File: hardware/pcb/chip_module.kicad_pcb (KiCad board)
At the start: 6 copper layers, 150 x 140 mm, 201 parts, among them J12 BTB_DAUGHTER

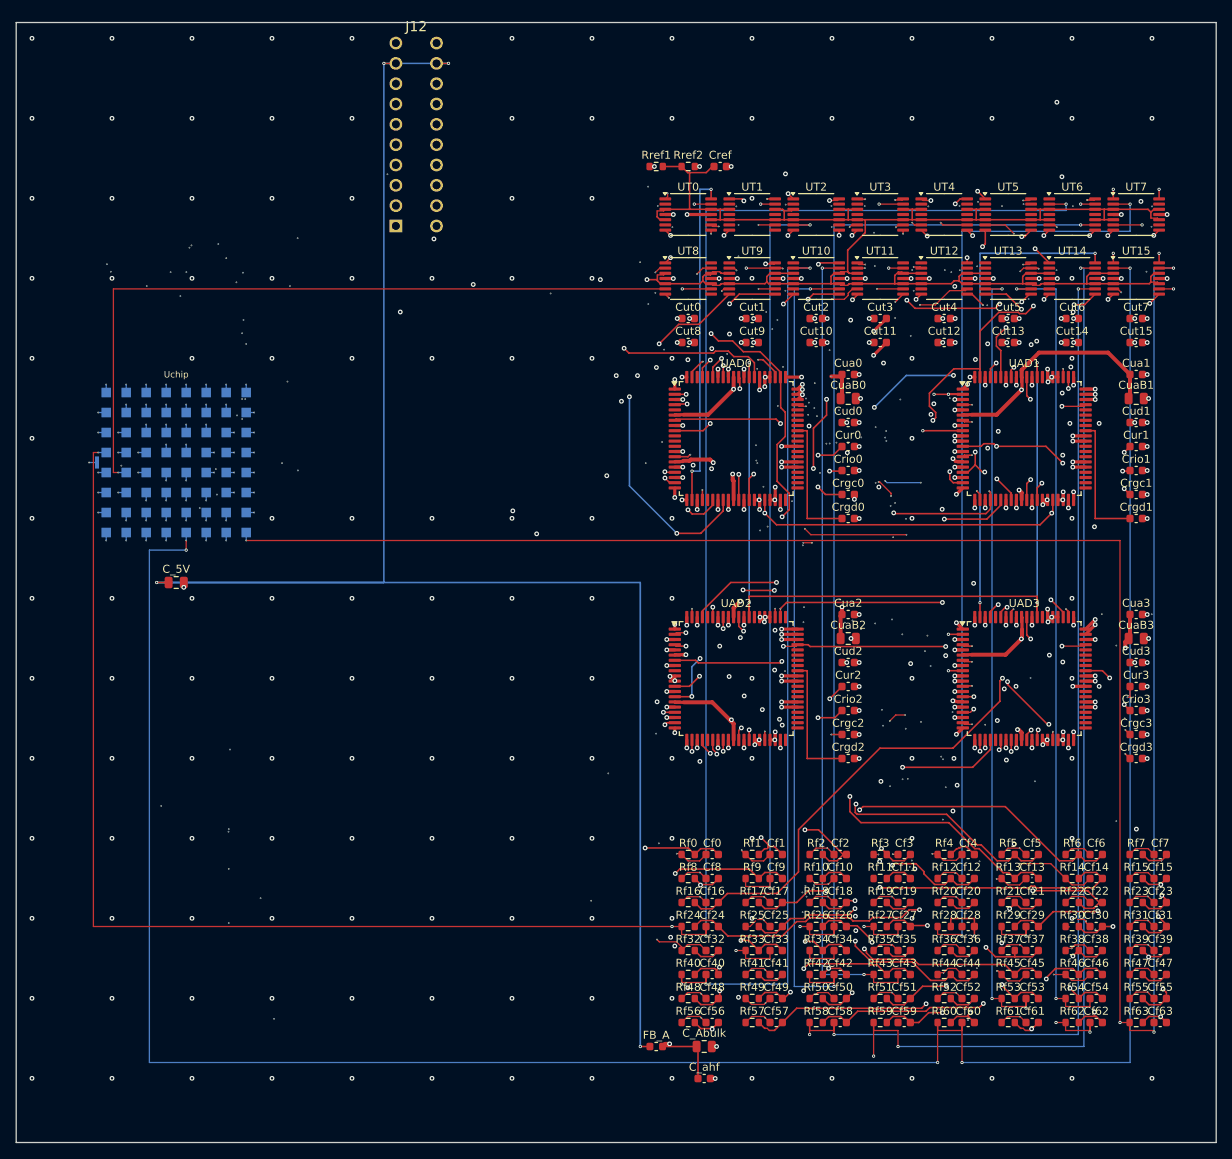
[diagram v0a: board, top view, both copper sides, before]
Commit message: pcb(head): FreeRouting cycle 1 -> 139->79 split nets, DRC 0/0/0
FreeRouting 2.4.1 -mt 0 -mp 6 on the head board (worktree off pcb/head-drc-clean).
Auto-routed the 301 unrouted items -> 92 internal; after SES import + fresh
zone re-fill the real gate (_split_nets) drops 139 -> 79 split nets (all 17
adc_* closed + 43 DET_* closed; 79 DET_* remain for cycle 2).

Post-cycle cleanup (freeroute.py imports the SES; this is the fresh-process
pass after):
  - widen 32 FreeRouting sub-min tracks (0.1124 mm -> 0.15 mm Chip netclass min)
  - relax min_hole_to_hole 0.22 -> 0.20 mm (HDI-safe; 2 adjacent FreeRouting
    fanout vias DET_IN11/DET_IN18 sit 0.2034 mm apart, 0.20 clears it)

DRC: 0 violations / 0 unconnected. Ruff clean.

Co-Authored-By: Claude Code <noreply@anthropic.com>
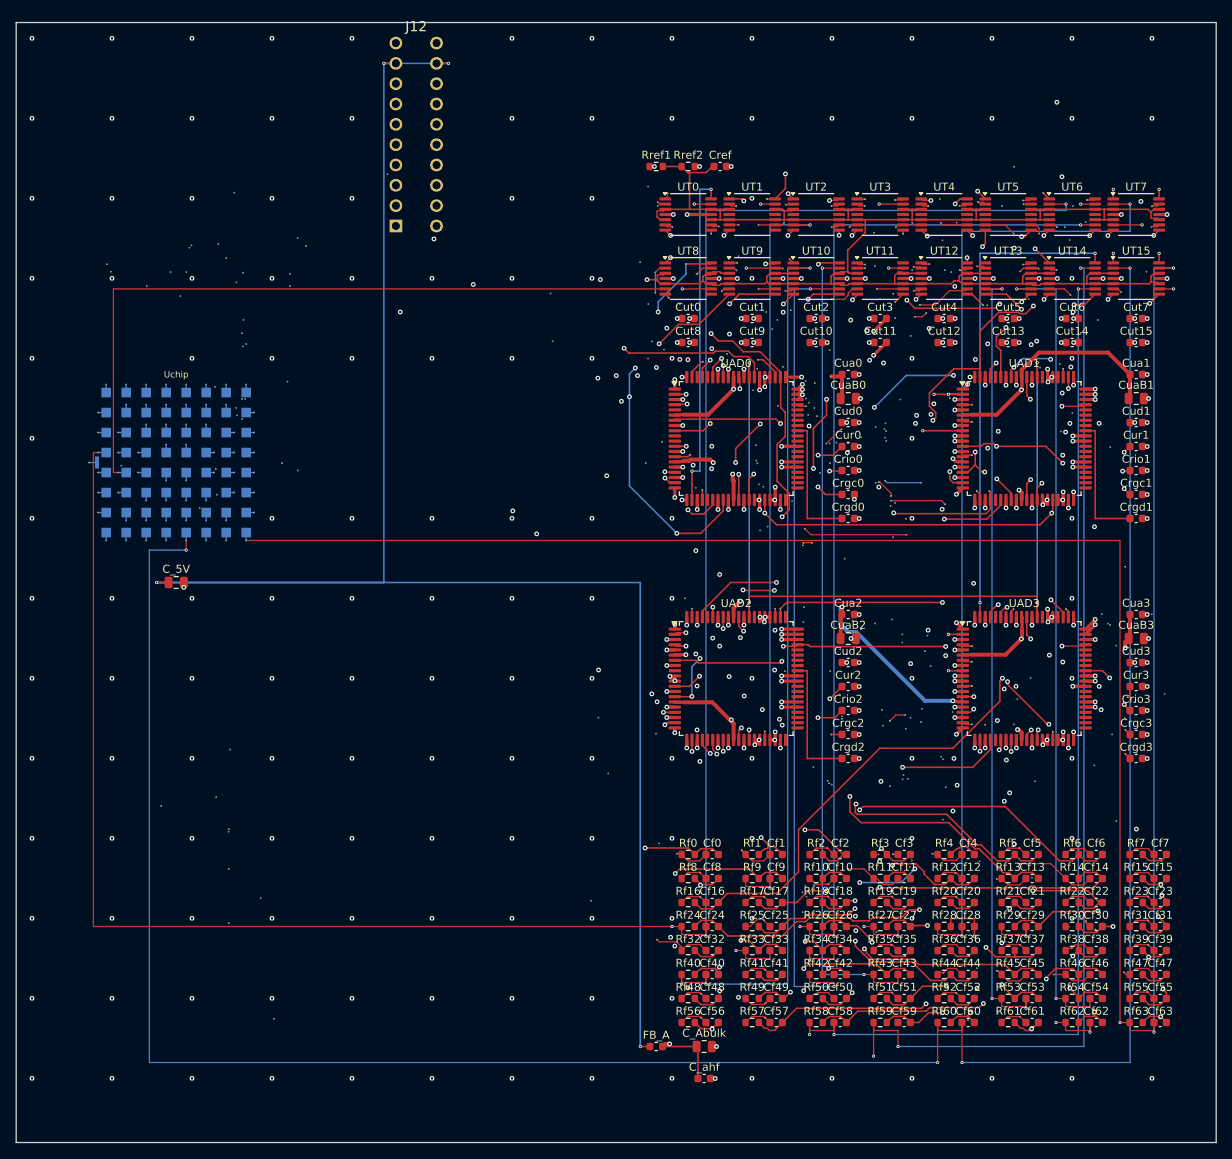
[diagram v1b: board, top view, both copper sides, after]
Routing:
- net DET_IN22: track 4.67 -> 237.7 mm, vias 1 -> 9
- net DET_IN56: track 100.7 -> 263.3 mm, vias 7 -> 9
- net DET_TIA15: track 38.2 -> 187.0 mm
- net DET_IN0: track 21.4 -> 169.9 mm, vias 3 -> 9
- net DET_IN57: track 111.6 -> 258.2 mm, vias 4 -> 11
- net DET_IN6: track 76.0 -> 211.9 mm, vias 3 -> 12
- net DET_IN55: track 102.0 -> 233.1 mm, vias 8 -> 12
- net DET_TIA7: track 50.5 -> 180.9 mm, vias 4 -> 6
- net DET_IN35: track 78.4 -> 194.2 mm, vias 8 -> 11
- net DET_IN11: track 88.5 -> 203.4 mm, vias 3 -> 8
- net DET_IN8: track 166.6 -> 281.5 mm, vias 7 -> 11
- net DET_TIA35: track 4.99 -> 117.8 mm, vias 2 -> 5
- net DET_IN16: track 124.2 -> 234.9 mm, vias 10 -> 14
- net DET_IN32: track 77.8 -> 185.7 mm
- net DET_IN30: track 135.9 -> 242.2 mm, vias 5 -> 8
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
